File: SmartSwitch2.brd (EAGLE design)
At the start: 100 x 50 mm, 24 parts

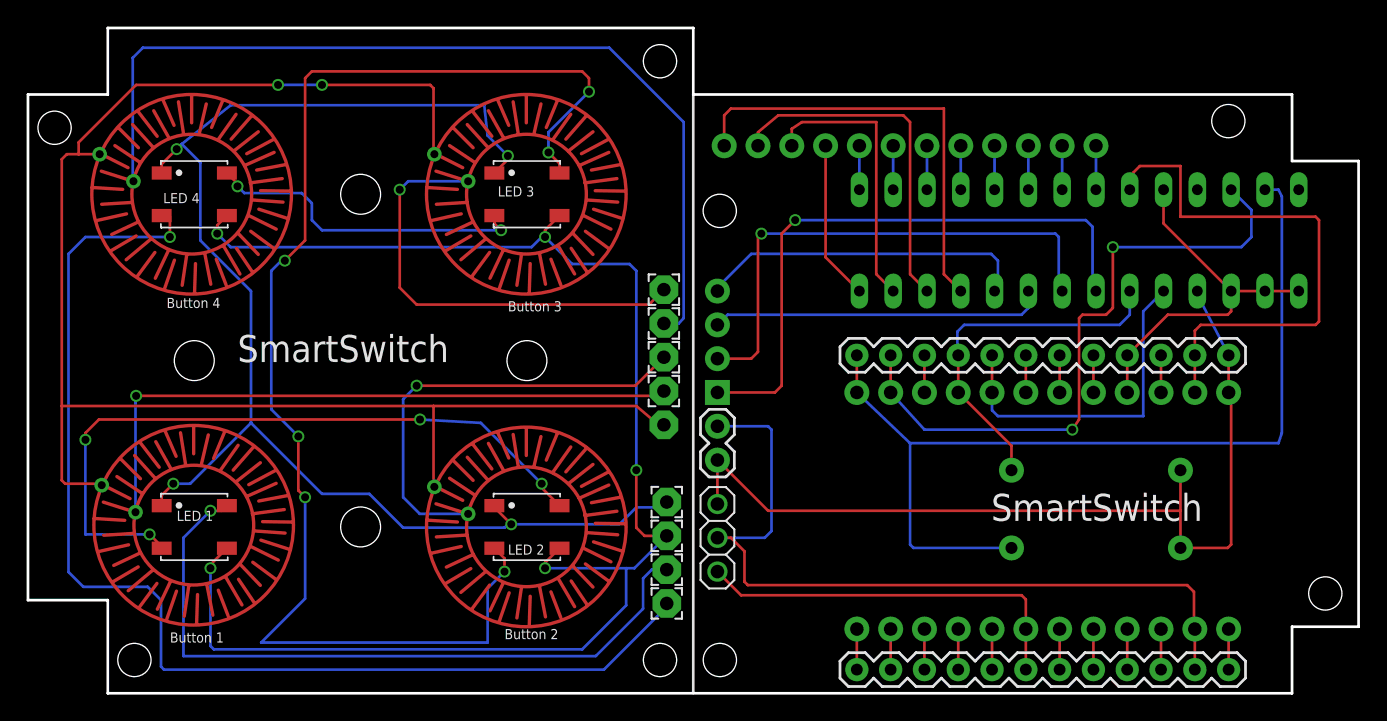
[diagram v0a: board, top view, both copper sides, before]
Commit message: series resistor, edges
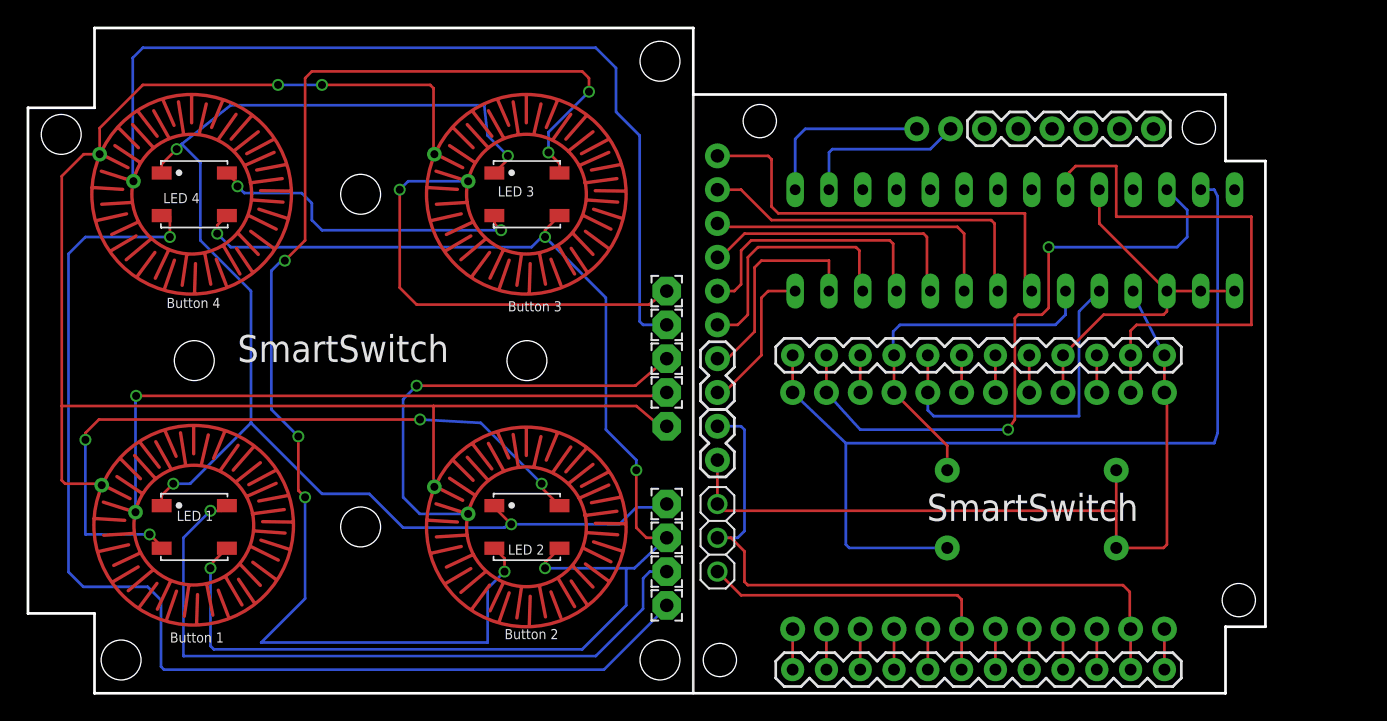
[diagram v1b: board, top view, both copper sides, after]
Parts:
- removed 5...16: (no value), SparkFun-Connectors:1X12
- added JP1: (no value), SparkFun-Connectors:1X06
- added JP3, JP7: M02PTH, SparkFun-Connectors:1X02
- BUTTONPAD: device SparkFun-Connectors:1X04 -> SparkFun-Connectors:1X06
- moved BUTTONPAD 17.8 mm to (51.8, 40.4), turned to 270 degrees
- moved JP4 4.83 mm to (57.5, 1.78)
- moved JP5 4.83 mm to (57.5, 25.4)
- moved MCP23017 4.83 mm to (74.2, 34.0)
- moved R1 4.83 mm to (75.4, 10.9)
- moved R2 4.83 mm to (75.4, 16.8)
- moved SPARK 4.83 mm to (71.4, 13.7)
- moved BTN2 0.24 mm to (48.0, 25.1)
- moved BTN3 0.24 mm to (48.0, 27.7)
- moved BTN4 0.24 mm to (48.0, 30.2)
- moved SWITCH 0.24 mm to (48.0, 20.1)
- moved BTN1 0.24 mm to (48.0, 22.6)
- moved GND 0.15 mm to (48.0, 11.7)
- moved OUT 0.15 mm to (48.0, 6.60)
- moved MOSI 0.15 mm to (48.0, 9.14)
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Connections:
- removed net N$20: 5...16.7, MCP23017.3
- removed net N$21: 5...16.8, MCP23017.4
- removed net N$22: 5...16.9, MCP23017.5
- removed net N$23: 5...16.10, MCP23017.6
- removed net N$24: 5...16.11, MCP23017.7
- removed net N$25: 5...16.12, MCP23017.8
- net N$14: now also BUTTONPAD.5; no longer 5...16.1
- net N$15: now also BUTTONPAD.6; no longer 5...16.2
- net N$16: now also JP7.1; no longer 5...16.3
- net N$17: now also JP7.2; no longer 5...16.4
- net N$18: now also JP3.1; no longer 5...16.5
- net N$19: now also JP3.2; no longer 5...16.6
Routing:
- net N$14: track 33.2 -> 20.0 mm
- net N$5: track 45.4 -> 33.0 mm, vias 1 -> 0
- net N$6: track 38.9 -> 27.1 mm, vias 1 -> 0
- net N$18: track 3.30 -> 13.3 mm
- net N$19: track 3.30 -> 12.7 mm
- net N$30: track 60.8 -> 51.9 mm
- net N$15: track 26.3 -> 18.9 mm
- net N$28: track 69.1 -> 63.1 mm
- net N$29: track 29.3 -> 24.5 mm
- net N$16: track 21.0 -> 16.5 mm
- net N$8: track 25.0 -> 20.8 mm
- net N$25: track 3.30 -> 0.00 mm
- net N$24: track 3.30 -> 0.00 mm
- net N$23: track 3.30 -> 0.00 mm
- net N$22: track 3.30 -> 0.00 mm
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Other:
- board size 100 x 50 mm -> 93 x 50 mm

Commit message: Change Jumper
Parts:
- removed LEDS: (no value), adafruit:1X03
- added JP6: (no value), SparkFun-Connectors:1X03
- moved JP1 12.7 mm to (71.9, 42.4), turned to 0 degrees
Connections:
- net N$28: now also JP6.3; no longer LEDS.1
- net N$29: now also JP6.1; no longer LEDS.3
- net N$30: now also JP6.2; no longer LEDS.2
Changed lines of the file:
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@@
 <attribute name="VALUE" x="58.42" y="34.9758" size="1.778" layer="28" ratio="10" rot="MR180"/>
-</element>
-<element name="LEDS" library="adafruit" package="1X03" value="" x="51.816" y="11.684" smashed="yes" rot="R270">
-<attribute name="VALUE" x="48.641" y="15.494" size="1.27" layer="27" rot="R270"/>
 </element>
 <element name="R1" library="SparkFun-Passives" package="AXIAL-0.5" value="" x="75.438" y="10.922" smashed="yes" rot="SMR0">
@@
 <attribute name="VALUE" x="78.867" y="16.383" size="0.8128" layer="22" font="vector" ratio="15" rot="SMR0"/>
 </element>
-<element name="BUTTONPAD" library="SparkFun-Connectors" package="1X06" value="" x="51.816" y="40.386" smashed="yes" rot="MR270">
-<attribute name="VALUE" x="49.911" y="41.656" size="1.27" layer="28" rot="MR270"/>
-<attribute name="PROD_ID" value="CONN-08437" x="51.816" y="40.386" size="1.778" layer="28" rot="MR270" display="off"/>
+<element name="BUTTONPAD" library="SparkFun-Connectors" package="1X06" value="" x="51.816" y="40.386" smashed="yes" rot="SMR270">
+<attribute name="VALUE" x="49.911" y="41.656" size="1.27" layer="28" rot="SMR270"/>
+<attribute name="PROD_ID" value="CONN-08437" x="51.816" y="40.386" size="1.778" layer="28" rot="SMR270" display="off"/>
 </element>
 <element name="SPARK" library="Spark" package="SPARK_CORE" value="SPARK_CORECORE" x="71.438" y="13.716" smashed="yes" rot="MR90">
@@
 <attribute name="VALUE" x="48.006" y="19.066" size="0.0254" layer="28" rot="MR180"/>
 </element>
-<element name="JP2" library="SparkFun-Connectors" package="1X02" value="M02PTH" x="51.816" y="20.066" smashed="yes" rot="R270"/>
-<element name="JP1" library="SparkFun-Connectors" package="1X06" value="" x="84.582" y="42.418" smashed="yes" rot="R180">
-<attribute name="PROD_ID" value="CONN-08437" x="84.582" y="42.418" size="1.778" layer="27" rot="R180" display="off"/>
-<attribute name="VALUE" x="85.852" y="45.593" size="1.27" layer="27" rot="R180"/>
-</element>
-<element name="JP3" library="SparkFun-Connectors" package="1X02" value="M02PTH" x="66.802" y="42.418" smashed="yes" rot="MR180"/>
+<element name="JP2" library="SparkFun-Connectors" package="1X02" value="M02PTH" x="51.816" y="20.066" smashed="yes" rot="SR270"/>
+<element name="JP1" library="SparkFun-Connectors" package="1X06" value="" x="71.882" y="42.418" smashed="yes" rot="SR0">
+<attribute name="PROD_ID" value="CONN-08437" x="71.882" y="42.418" size="1.778" layer="27" rot="SR0" display="off"/>
+<attribute name="VALUE" x="70.612" y="39.243" size="1.27" layer="27" rot="SR0"/>
+</element>
+<element name="JP3" library="SparkFun-Connectors" package="1X02" value="M02PTH" x="66.802" y="42.418" smashed="yes" rot="SMR180"/>
 <element name="JP7" library="SparkFun-Connectors" package="1X02" value="M02PTH" x="51.816" y="25.146" smashed="yes" rot="R270"/>
+<element name="JP6" library="SparkFun-Connectors" package="1X03" value="" x="51.816" y="9.144" smashed="yes" rot="SR90">
+<attribute name="VALUE" x="54.991" y="7.874" size="1.27" layer="27" rot="SR90"/>
+</element>
 </elements>
 <signals>
@@
 <contactref element="JP5" pad="12"/>
 <contactref element="JP2" pad="2"/>
-<contactref element="LEDS" pad="1"/>
 <wire x1="85.408" y1="25.4" x2="83.058" y2="29.972" width="0.2032" layer="16"/>
 <wire x1="83.058" y1="29.972" x2="83.058" y2="30.226" width="0.2032" layer="16"/>
@@
 <wire x1="52.07" y1="13.716" x2="81.788" y2="13.716" width="0.2032" layer="1"/>
 <wire x1="52.07" y1="13.716" x2="51.816" y2="13.97" width="0.2032" layer="1"/>
+<contactref element="JP6" pad="3"/>
 <wire x1="51.816" y1="13.97" x2="51.816" y2="14.224" width="0.2032" layer="1"/>
 <wire x1="51.816" y1="17.526" x2="51.816" y2="14.224" width="0.2032" layer="1"/>
 </signal>
 <signal name="N$29">
-<contactref element="LEDS" pad="3"/>
 <contactref element="SPARK" pad="7"/>
 <contactref element="JP4" pad="6"/>
 <wire x1="70.168" y1="4.826" x2="70.168" y2="1.778" width="0.2032" layer="1"/>
-<wire x1="51.816" y1="9.144" x2="53.594" y2="7.366" width="0.2032" layer="1"/>
 <wire x1="53.594" y1="7.366" x2="69.85" y2="7.366" width="0.2032" layer="1"/>
 <wire x1="69.85" y1="7.366" x2="70.168" y2="7.048" width="0.2032" layer="1"/>
 <wire x1="70.168" y1="7.048" x2="70.168" y2="4.826" width="0.2032" layer="1"/>
+<contactref element="JP6" pad="1"/>
+<wire x1="53.594" y1="7.366" x2="51.816" y2="9.144" width="0.2032" layer="1"/>
 </signal>
 <signal name="N$30">
-<contactref element="LEDS" pad="2"/>
 <contactref element="SPARK" pad="2"/>
 <contactref element="JP4" pad="11"/>
 <wire x1="82.868" y1="4.826" x2="82.868" y2="1.778" width="0.2032" layer="1"/>
 <contactref element="JP2" pad="1"/>
-<wire x1="51.816" y1="11.684" x2="53.34" y2="11.684" width="0.2032" layer="16"/>
 <wire x1="53.34" y1="11.684" x2="53.848" y2="12.192" width="0.2032" layer="16"/>
 <wire x1="53.848" y1="12.192" x2="53.848" y2="19.812" width="0.2032" layer="16"/>
@@
 <wire x1="53.848" y1="8.382" x2="53.848" y2="10.668" width="0.2032" layer="1"/>
 <wire x1="53.848" y1="10.668" x2="52.832" y2="11.684" width="0.2032" layer="1"/>
+<contactref element="JP6" pad="2"/>
 <wire x1="52.832" y1="11.684" x2="51.816" y2="11.684" width="0.2032" layer="1"/>
+<wire x1="53.34" y1="11.684" x2="51.816" y2="11.684" width="0.2032" layer="16"/>
 </signal>
 <signal name="N$32">

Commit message: Resistors
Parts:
- added R3, R4, R5, R6, R7, R8: (no value), SparkFun-Resistors:AXIAL-0.4
- R1, R2: device SparkFun-Passives:AXIAL-0.5 -> SparkFun-Resistors:AXIAL-0.4
- moved JP1 28.5 mm to (59.4, 16.8), flipped to the bottom, turned to 180 degrees
- moved R1 11.4 mm to (85.3, 16.5), turned to 180 degrees
- moved R2 10.3 mm to (85.3, 19.6), turned to 180 degrees
- moved JP3 7.62 mm to (59.2, 42.7)
- moved MCP23017 2.34 mm to (72.4, 35.6)
- flipped JP2 to the bottom
- flipped JP6 to the bottom
- flipped JP7 to the bottom
- flipped SWITCH to the top
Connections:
- new net N$20: MCP23017.3, R3.P$1
- new net N$21: JP1.1, R3.P$2
- new net N$22: JP1.2, R4.P$2
- new net N$23: JP1.3, R5.P$2
- new net N$24: JP1.4, R6.P$2
- new net N$25: JP1.5, R7.P$2
- new net N$45: JP1.6, R8.P$2
- new net N$52: MCP23017.8, R8.P$1
- new net N$53: MCP23017.7, R7.P$1
- new net N$54: MCP23017.6, R6.P$1
- new net N$55: MCP23017.5, R5.P$1
- new net N$56: MCP23017.4, R4.P$1
- net N$28: now also MCP23017.9
- net N$33: now also R2.P$2
- net N$49: no longer MCP23017.9
- net N$51: no longer R2.P$2
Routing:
- net N$49: track 41.1 -> 2.79 mm
- net N$33: track 48.6 -> 72.7 mm, vias 2 -> 1
- net N$32: track 28.3 -> 45.8 mm
- net N$12: track 101.5 -> 88.9 mm
- net N$56: track 0.00 -> 10.8 mm
- net N$55: track 0.00 -> 10.8 mm
- net N$54: track 0.00 -> 10.8 mm
- net N$53: track 0.00 -> 10.8 mm
- net N$52: track 0.00 -> 10.8 mm
- net N$20: track 0.00 -> 10.8 mm
- net N$18: track 13.3 -> 4.67 mm
- net N$19: track 12.7 -> 4.67 mm
- net N$51: track 27.4 -> 19.9 mm
- net N$27: track 25.7 -> 18.6 mm
- net N$5: track 33.0 -> 30.2 mm
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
